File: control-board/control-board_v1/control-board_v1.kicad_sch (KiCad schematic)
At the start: 57 parts, among them J1 Barrel_Jack, J2 Header-M_2x6, J3 Header-M_2x6, J4 Header-M_2x6, J5 Header-M_2x6, J6 Header_1x8, J7 Header_1x8, J8 Header_1x10, J9 Header_1x8, Q1 PMOS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

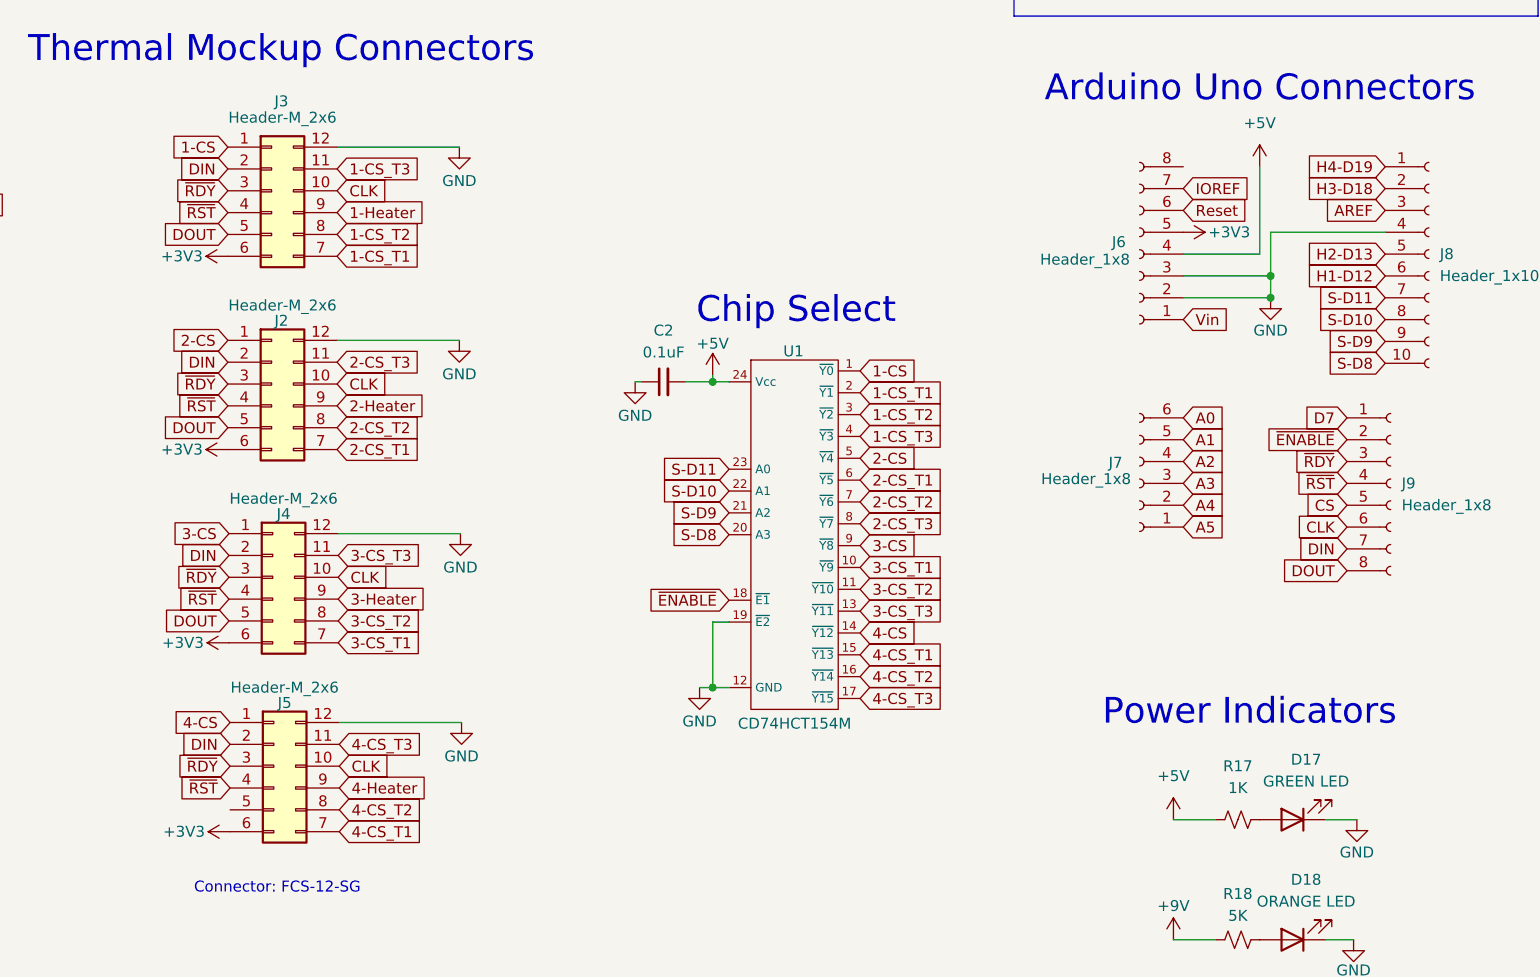
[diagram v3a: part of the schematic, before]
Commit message: added pcb layout
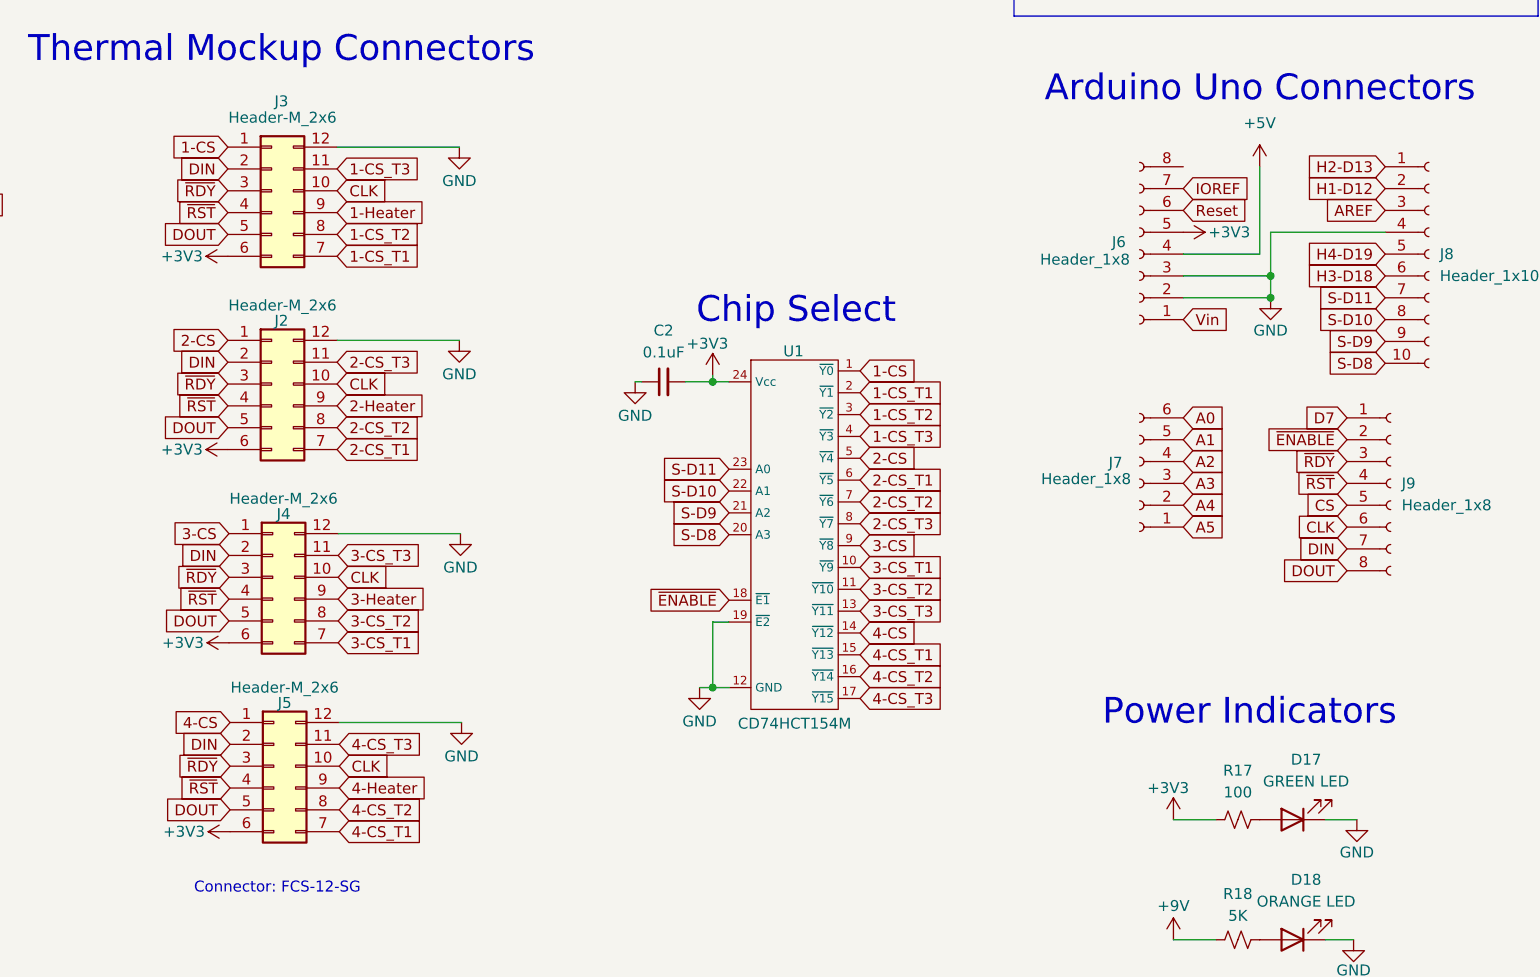
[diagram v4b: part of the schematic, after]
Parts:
- R17: value 1K -> 100
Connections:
- net +3V3: now also C2.2, R17.1, U1.24 (Vcc)
- net +5V: no longer C2.2, R17.1, U1.24 (Vcc)
- net DOUT: now also J5.5 (Pin_5)
- net H1-D12: now also J8.2 (Pin_2); no longer J8.6 (Pin_6)
- net H2-D13: now also J8.1 (Pin_1); no longer J8.5 (Pin_5)
- net H3-D18: now also J8.6 (Pin_6); no longer J8.2 (Pin_2)
- net H4-D19: now also J8.5 (Pin_5); no longer J8.1 (Pin_1)
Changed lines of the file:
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@@
     )
   )
+  (global_label "H3-D18" (shape input) (at 265.684 79.629 180) (fields_autoplaced)
+    (effects (font (size 1.27 1.27)) (justify right))
+    (property "Intersheetrefs" "${INTERSHEET_REFS}" (at 254.8974 79.629 0)
+      (effects (font (size 1.27 1.27)) (justify right) hide)
+    )
+  )
   (global_label "CLK" (shape input) (at 143.764 92.202 0) (fields_autoplaced)
     (effects (font (size 1.27 1.27)) (justify left))
@@
     )
   )
+  (global_label "H2-D13" (shape input) (at 265.684 66.929 180) (fields_autoplaced)
+    (effects (font (size 1.27 1.27)) (justify right))
+    (property "Intersheetrefs" "${INTERSHEET_REFS}" (at 254.8974 66.929 0)
+      (effects (font (size 1.27 1.27)) (justify right) hide)
+    )
+  )
   (global_label "2-CS_T2" (shape input) (at 143.764 97.282 0) (fields_autoplaced)
     (effects (font (size 1.27 1.27)) (justify left))
@@
     )
   )
+  (global_label "DOUT" (shape input) (at 131.318 141.732 180) (fields_autoplaced)
+    (effects (font (size 1.27 1.27)) (justify right))
+    (property "Intersheetrefs" "${INTERSHEET_REFS}" (at 123.4342 141.732 0)
+      (effects (font (size 1.27 1.27)) (justify right) hide)
+    )
+  )
   (global_label "4-CS" (shape input) (at 204.597 121.158 0) (fields_autoplaced)
     (effects (font (size 1.27 1.27)) (justify left))
@@
     )
   )
-  (global_label "H1-D12" (shape input) (at 265.684 79.629 180) (fields_autoplaced)
-    (effects (font (size 1.27 1.27)) (justify right))
-    (property "Intersheetrefs" "${INTERSHEET_REFS}" (at 254.8974 79.629 0)
-      (effects (font (size 1.27 1.27)) (justify right) hide)
-    )
-  )
   (global_label "Reset" (shape input) (at 242.189 72.009 0) (fields_autoplaced)
     (effects (font (size 1.27 1.27)) (justify left))
@@
     )
   )
-  (global_label "H3-D18" (shape input) (at 265.684 69.469 180) (fields_autoplaced)
-    (effects (font (size 1.27 1.27)) (justify right))
-    (property "Intersheetrefs" "${INTERSHEET_REFS}" (at 254.8974 69.469 0)
-      (effects (font (size 1.27 1.27)) (justify right) hide)
-    )
-  )
   (global_label "S-D9" (shape input) (at 189.357 107.188 180) (fields_autoplaced)
     (effects (font (size 1.27 1.27)) (justify right))
@@
     )
   )
-  (global_label "H4-D19" (shape input) (at 265.684 66.929 180) (fields_autoplaced)
-    (effects (font (size 1.27 1.27)) (justify right))
-    (property "Intersheetrefs" "${INTERSHEET_REFS}" (at 254.8974 66.929 0)
-      (effects (font (size 1.27 1.27)) (justify right) hide)
-    )
-  )
   (global_label "1-CS" (shape input) (at 204.597 90.678 0) (fields_autoplaced)
     (effects (font (size 1.27 1.27)) (justify left))
@@
     )
   )
-  (global_label "H2-D13" (shape input) (at 265.684 77.089 180) (fields_autoplaced)
-    (effects (font (size 1.27 1.27)) (justify right))
-    (property "Intersheetrefs" "${INTERSHEET_REFS}" (at 254.8974 77.089 0)
-      (effects (font (size 1.27 1.27)) (justify right) hide)
-    )
-  )
   (global_label "2-CS_T1" (shape input) (at 50.8 70.739 0) (fields_autoplaced)
     (effects (font (size 1.27 1.27)) (justify left))
@@
     )
   )
+  (global_label "H4-D19" (shape input) (at 265.684 77.089 180) (fields_autoplaced)
+    (effects (font (size 1.27 1.27)) (justify right))
+    (property "Intersheetrefs" "${INTERSHEET_REFS}" (at 254.8974 77.089 0)
+      (effects (font (size 1.27 1.27)) (justify right) hide)
+    )
+  )
   (global_label "4-CS" (shape input) (at 131.318 131.572 180) (fields_autoplaced)
     (effects (font (size 1.27 1.27)) (justify right))
@@
     )
   )
+  (global_label "H1-D12" (shape input) (at 265.684 69.469 180) (fields_autoplaced)
+    (effects (font (size 1.27 1.27)) (justify right))
+    (property "Intersheetrefs" "${INTERSHEET_REFS}" (at 254.8974 69.469 0)
+      (effects (font (size 1.27 1.27)) (justify right) hide)
+    )
+  )
   (global_label "AREF" (shape input) (at 265.684 72.009 180) (fields_autoplaced)
     (effects (font (size 1.27 1.27)) (justify right))
@@
   (symbol (lib_id "Device:R_Small_US") (at 248.539 142.875 90) (unit 1)
     (in_bom yes) (on_board yes) (dnp no) (fields_autoplaced)
-    (property "Reference" "R17" (at 248.539 136.652 90)
+    (property "Reference" "R17" (at 248.539 137.16 90)
       (effects (font (size 1.27 1.27)))
     )
-    (property "Value" "1K" (at 248.539 139.192 90)
+    (property "Value" "100" (at 248.539 139.7 90)
       (effects (font (size 1.27 1.27)))
     )
@@
     )
   )
+  (symbol (lib_id "power:+3V3") (at 241.046 142.875 0) (unit 1)
+    (in_bom yes) (on_board yes) (dnp no)
+    (property "Reference" "#PWR054" (at 241.046 146.685 0)
+      (effects (font (size 1.27 1.27)) hide)
+    )
+    (property "Value" "+3V3" (at 237.998 139.192 0)
+      (effects (font (size 1.27 1.27)) (justify left))
+    )
+    (property "Footprint" "" (at 241.046 142.875 0)
+      (effects (font (size 1.27 1.27)) hide)
+    )
+    (property "Datasheet" "" (at 241.046 142.875 0)
+      (effects (font (size 1.27 1.27)) hide)
+    )
+    (pin "1")
+    (instances
+      (project "control-board_v1"
+        (path "/5ea0e920-d127-456d-9ad4-df9bbc649b9b"
+          (reference "#PWR054") (unit 1)
+        )
+      )
+      (project "arduino_uno"
+        (path "/b1128066-0aeb-425d-915d-968e839977c3"
+          (reference "#PWR030") (unit 1)
+        )
+      )
+    )
+  )
   (symbol (lib_id "Connector:Conn_01x08_Socket") (at 266.319 103.759 0) (unit 1)
     (in_bom yes) (on_board yes) (dnp no) (fields_autoplaced)
@@
     )
   )
-  (symbol (lib_id "power:+5V") (at 187.452 91.186 0) (unit 1)
-    (in_bom yes) (on_board yes) (dnp no)
-    (property "Reference" "#PWR036" (at 187.452 94.996 0)
-      (effects (font (size 1.27 1.27)) hide)
-    )
-    (property "Value" "+5V" (at 187.452 87.503 0)
-      (effects (font (size 1.27 1.27)))
-    )
-    (property "Footprint" "" (at 187.452 91.186 0)
-      (effects (font (size 1.27 1.27)) hide)
-    )
-    (property "Datasheet" "" (at 187.452 91.186 0)
-      (effects (font (size 1.27 1.27)) hide)
-    )
-    (pin "1")
-    (instances
-      (project "control-board_v1"
-        (path "/5ea0e920-d127-456d-9ad4-df9bbc649b9b"
-          (reference "#PWR036") (unit 1)
-        )
-      )
-    )
-  )
   (symbol (lib_id "Device:Q_Dual_PMOS_S1G1D2S2G2D1") (at 23.622 61.341 180) (unit 2)
     (in_bom yes) (on_board yes) (dnp no) (fields_autoplaced)
@@
     )
   )
+  (symbol (lib_id "power:+3V3") (at 187.452 91.186 0) (unit 1)
+    (in_bom yes) (on_board yes) (dnp no)
+    (property "Reference" "#PWR036" (at 187.452 94.996 0)
+      (effects (font (size 1.27 1.27)) hide)
+    )
+    (property "Value" "+3V3" (at 184.404 87.503 0)
+      (effects (font (size 1.27 1.27)) (justify left))
+    )
+    (property "Footprint" "" (at 187.452 91.186 0)
+      (effects (font (size 1.27 1.27)) hide)
+    )
+    (property "Datasheet" "" (at 187.452 91.186 0)
+      (effects (font (size 1.27 1.27)) hide)
+    )
+    (pin "1")
+    (instances
+      (project "control-board_v1"
+        (path "/5ea0e920-d127-456d-9ad4-df9bbc649b9b"
+          (reference "#PWR036") (unit 1)
+        )
+      )
+      (project "arduino_uno"
+        (path "/b1128066-0aeb-425d-915d-968e839977c3"
+          (reference "#PWR030") (unit 1)
+        )
+      )
+    )
+  )
   (symbol (lib_id "power:GND") (at 65.278 150.241 0) (unit 1)
     (in_bom yes) (on_board yes) (dnp no)
@@
         )
       )
-    )
-  )
-  (symbol (lib_id "power:+5V") (at 241.046 142.875 0) (unit 1)
-    (in_bom yes) (on_board yes) (dnp no) (fields_autoplaced)
-    (property "Reference" "#PWR062" (at 241.046 146.685 0)
-      (effects (font (size 1.27 1.27)) hide)
-    )
-    (property "Value" "+5V" (at 241.046 137.795 0)
-      (effects (font (size 1.27 1.27)))
-    )
-    (property "Footprint" "" (at 241.046 142.875 0)
-      (effects (font (size 1.27 1.27)) hide)
-    )
-    (property "Datasheet" "" (at 241.046 142.875 0)
-      (effects (font (size 1.27 1.27)) hide)
-    )
-    (pin "1")
-    (instances
-      (project "control-board_v1"
-        (path "/5ea0e920-d127-456d-9ad4-df9bbc649b9b"
-          (reference "#PWR062") (unit 1)
-        )
-      )

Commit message: pcb design change
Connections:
- net GND: no longer J2.12 (Pin_12), J3.12 (Pin_12), J4.12 (Pin_12), J5.12 (Pin_12)
- net H1-D12: now also J8.1 (Pin_1); no longer J8.2 (Pin_2)
- net H2-D13: now also J8.2 (Pin_2); no longer J8.1 (Pin_1)
- new net 1-GND: J3.12 (Pin_12)
- new net 2-GND: J2.12 (Pin_12)
- new net 3-GND: J4.12 (Pin_12)
- new net 4-GND: J5.12 (Pin_12)
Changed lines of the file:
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@@
   )
   (no_connect (at 100.457 118.491))
-  (wire (pts (xy 158.115 109.601) (xy 143.891 109.601))
-    (stroke (width 0) (type default))
-  )
   (wire (pts (xy 179.197 91.948) (xy 178.435 91.948))
     (stroke (width 0) (type default))
@@
     (stroke (width 0) (type default))
   )
-  (wire (pts (xy 157.988 87.122) (xy 143.764 87.122))
-    (stroke (width 0) (type default))
-  )
   (wire (pts (xy 249.936 36.449) (xy 253.492 36.449))
     (stroke (width 0) (type default))
@@
     (stroke (width 0) (type default))
   )
-  (wire (pts (xy 157.988 64.643) (xy 143.764 64.643))
-    (stroke (width 0) (type default))
-  )
   (wire (pts (xy 187.452 91.948) (xy 189.357 91.948))
     (stroke (width 0) (type default))
@@
     (stroke (width 0) (type default))
   )
-  (wire (pts (xy 158.242 131.572) (xy 144.018 131.572))
-    (stroke (width 0) (type default))
-  )
   (wire (pts (xy 187.452 127.508) (xy 189.357 127.508))
     (stroke (width 0) (type default))
@@
     )
   )
-  (global_label "H2-D13" (shape input) (at 265.684 66.929 180) (fields_autoplaced)
-    (effects (font (size 1.27 1.27)) (justify right))
-    (property "Intersheetrefs" "${INTERSHEET_REFS}" (at 254.8974 66.929 0)
-      (effects (font (size 1.27 1.27)) (justify right) hide)
+  (global_label "1-GND" (shape input) (at 143.764 64.643 0) (fields_autoplaced)
+    (effects (font (size 1.27 1.27)) (justify left))
+    (property "Intersheetrefs" "${INTERSHEET_REFS}" (at 153.4016 64.643 0)
+      (effects (font (size 1.27 1.27)) (justify left) hide)
     )
   )
@@
     )
   )
+  (global_label "4-GND" (shape input) (at 144.018 131.572 0) (fields_autoplaced)
+    (effects (font (size 1.27 1.27)) (justify left))
+    (property "Intersheetrefs" "${INTERSHEET_REFS}" (at 153.6556 131.572 0)
+      (effects (font (size 1.27 1.27)) (justify left) hide)
+    )
+  )
   (global_label "1-CS" (shape input) (at 204.597 90.678 0) (fields_autoplaced)
     (effects (font (size 1.27 1.27)) (justify left))
@@
     )
   )
+  (global_label "H1-D12" (shape input) (at 265.684 66.929 180) (fields_autoplaced)
+    (effects (font (size 1.27 1.27)) (justify right))
+    (property "Intersheetrefs" "${INTERSHEET_REFS}" (at 254.8974 66.929 0)
+      (effects (font (size 1.27 1.27)) (justify right) hide)
+    )
+  )
   (global_label "S-D8" (shape input) (at 189.357 109.728 180) (fields_autoplaced)
     (effects (font (size 1.27 1.27)) (justify right))
@@
     )
   )
+  (global_label "H2-D13" (shape input) (at 265.684 69.469 180) (fields_autoplaced)
+    (effects (font (size 1.27 1.27)) (justify right))
+    (property "Intersheetrefs" "${INTERSHEET_REFS}" (at 254.8974 69.469 0)
+      (effects (font (size 1.27 1.27)) (justify right) hide)
+    )
+  )
   (global_label "CLK" (shape input) (at 261.239 108.839 180) (fields_autoplaced)
     (effects (font (size 1.27 1.27)) (justify right))
@@
     )
   )
+  (global_label "3-GND" (shape input) (at 143.891 109.601 0) (fields_autoplaced)
+    (effects (font (size 1.27 1.27)) (justify left))
+    (property "Intersheetrefs" "${INTERSHEET_REFS}" (at 153.5286 109.601 0)
+      (effects (font (size 1.27 1.27)) (justify left) hide)
+    )
+  )
   (global_label "1-CS_T2" (shape input) (at 143.764 74.803 0) (fields_autoplaced)
     (effects (font (size 1.27 1.27)) (justify left))
@@
     )
   )
-  (global_label "H1-D12" (shape input) (at 265.684 69.469 180) (fields_autoplaced)
-    (effects (font (size 1.27 1.27)) (justify right))
-    (property "Intersheetrefs" "${INTERSHEET_REFS}" (at 254.8974 69.469 0)
-      (effects (font (size 1.27 1.27)) (justify right) hide)
-    )
-  )
   (global_label "AREF" (shape input) (at 265.684 72.009 180) (fields_autoplaced)
     (effects (font (size 1.27 1.27)) (justify right))
@@
     )
   )
+  (global_label "2-GND" (shape input) (at 143.764 87.122 0) (fields_autoplaced)
+    (effects (font (size 1.27 1.27)) (justify left))
+    (property "Intersheetrefs" "${INTERSHEET_REFS}" (at 153.4016 87.122 0)
+      (effects (font (size 1.27 1.27)) (justify left) hide)
+    )
+  )
   (global_label "~{RDY}" (shape input) (at 131.064 92.202 180) (fields_autoplaced)
     (effects (font (size 1.27 1.27)) (justify right))
@@
     )
   )
-  (symbol (lib_id "power:GND") (at 158.115 109.601 0) (unit 1)
-    (in_bom yes) (on_board yes) (dnp no)
-    (property "Reference" "#PWR048" (at 158.115 115.951 0)
-      (effects (font (size 1.27 1.27)) hide)
-    )
-    (property "Value" "GND" (at 158.115 113.538 0)
-      (effects (font (size 1.27 1.27)))
-    )
-    (property "Footprint" "" (at 158.115 109.601 0)
-      (effects (font (size 1.27 1.27)) hide)
-    )
-    (property "Datasheet" "" (at 158.115 109.601 0)
-      (effects (font (size 1.27 1.27)) hide)
-    )
-    (pin "1")
-    (instances
-      (project "control-board_v1"
-        (path "/5ea0e920-d127-456d-9ad4-df9bbc649b9b"
-          (reference "#PWR048") (unit 1)
-        )
-      )
-    )
-  )
   (symbol (lib_id "Connector_Generic:Conn_02x06_Counter_Clockwise") (at 136.398 136.652 0) (unit 1)
     (in_bom yes) (on_board yes) (dnp no)
@@
     )
   )
-  (symbol (lib_id "power:GND") (at 157.988 87.122 0) (unit 1)
-    (in_bom yes) (on_board yes) (dnp no)
-    (property "Reference" "#PWR047" (at 157.988 93.472 0)
-      (effects (font (size 1.27 1.27)) hide)
-    )
-    (property "Value" "GND" (at 157.988 91.059 0)
-      (effects (font (size 1.27 1.27)))
-    )
-    (property "Footprint" "" (at 157.988 87.122 0)
-      (effects (font (size 1.27 1.27)) hide)
-    )
-    (property "Datasheet" "" (at 157.988 87.122 0)
-      (effects (font (size 1.27 1.27)) hide)
-    )
-    (pin "1")
-    (instances
-      (project "control-board_v1"
-        (path "/5ea0e920-d127-456d-9ad4-df9bbc649b9b"
-          (reference "#PWR047") (unit 1)
-        )
-      )
-    )
-  )
   (symbol (lib_id "power:+9V") (at 241.046 156.845 0) (unit 1)
     (in_bom yes) (on_board yes) (dnp no)
@@
     )
   )
-  (symbol (lib_id "power:GND") (at 157.988 64.643 0) (unit 1)
-    (in_bom yes) (on_board yes) (dnp no)
-    (property "Reference" "#PWR046" (at 157.988 70.993 0)
-      (effects (font (size 1.27 1.27)) hide)
-    )
-    (property "Value" "GND" (at 157.988 68.58 0)
-      (effects (font (size 1.27 1.27)))
-    )
-    (property "Footprint" "" (at 157.988 64.643 0)
-      (effects (font (size 1.27 1.27)) hide)
-    )
-    (property "Datasheet" "" (at 157.988 64.643 0)
-      (effects (font (size 1.27 1.27)) hide)
-    )
-    (pin "1")
-    (instances
-      (project "control-board_v1"
-        (path "/5ea0e920-d127-456d-9ad4-df9bbc649b9b"
-          (reference "#PWR046") (unit 1)
-        )
-      )
-    )
-  )
   (symbol (lib_id "Device:LED") (at 42.799 119.253 90) (unit 1)
     (in_bom yes) (on_board yes) (dnp no) (fields_autoplaced)
@@
         )
       )
-    )
-  )
-  (symbol (lib_id "power:GND") (at 158.242 131.572 0) (unit 1)
-    (in_bom yes) (on_board yes) (dnp no)
-    (property "Reference" "#PWR049" (at 158.242 137.922 0)
-      (effects (font (size 1.27 1.27)) hide)
-    )
-    (property "Value" "GND" (at 158.242 135.509 0)
-      (effects (font (size 1.27 1.27)))
-    )
-    (property "Footprint" "" (at 158.242 131.572 0)
-      (effects (font (size 1.27 1.27)) hide)
-    )
-    (property "Datasheet" "" (at 158.242 131.572 0)
-      (effects (font (size 1.27 1.27)) hide)
-    )
-    (pin "1")
-    (instances
-      (project "control-board_v1"
-        (path "/5ea0e920-d127-456d-9ad4-df9bbc649b9b"
-          (reference "#PWR049") (unit 1)
-        )
-      )
